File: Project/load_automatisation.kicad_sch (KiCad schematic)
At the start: 9 parts, among them IC3 MC74VHC138DR2G, J10 DadConnector, J11 TENG, J9 PowerIn, U1 AMS1117-5.0

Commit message: new schematic
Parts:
- IC3: footprint SOIC127P600X175-16N -> Library:SOIC127P600X175-16N
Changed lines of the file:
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@@
 	(wire
 		(pts
-			(xy 105.41 74.93) (xy 107.95 74.93)
-		)
-		(stroke
-			(width 0)
-			(type default)
-		)
-	)
-	(wire
-		(pts
-			(xy 102.87 64.77) (xy 107.95 64.77)
+			(xy 101.6 74.93) (xy 107.95 74.93)
 		)
 		(stroke
@@
 	(wire
 		(pts
-			(xy 102.87 69.85) (xy 107.95 69.85)
-		)
-		(stroke
-			(width 0)
-			(type default)
-		)
-	)
-	(wire
-		(pts
 			(xy 107.95 77.47) (xy 104.14 77.47)
 		)
@@
 	(wire
 		(pts
+			(xy 99.06 67.31) (xy 107.95 67.31)
+		)
+		(stroke
+			(width 0)
+			(type default)
+		)
+	)
+	(wire
+		(pts
 			(xy 115.57 39.37) (xy 115.57 36.83)
 		)
@@
 	(wire
 		(pts
-			(xy 102.87 67.31) (xy 107.95 67.31)
-		)
-		(stroke
-			(width 0)
-			(type default)
-		)
-	)
-	(wire
-		(pts
 			(xy 41.91 40.64) (xy 58.42 40.64)
 		)
@@
 	(wire
 		(pts
-			(xy 102.87 72.39) (xy 107.95 72.39)
-		)
-		(stroke
-			(width 0)
-			(type default)
-		)
-	)
-	(wire
-		(pts
-			(xy 102.87 59.69) (xy 107.95 59.69)
-		)
-		(stroke
-			(width 0)
-			(type default)
-		)
-	)
-	(wire
-		(pts
 			(xy 35.56 68.58) (xy 44.45 68.58)
 		)
@@
 	(wire
 		(pts
+			(xy 99.06 69.85) (xy 107.95 69.85)
+		)
+		(stroke
+			(width 0)
+			(type default)
+		)
+	)
+	(wire
+		(pts
 			(xy 58.42 40.64) (xy 58.42 38.1)
 		)
@@
 	(wire
 		(pts
+			(xy 99.06 62.23) (xy 107.95 62.23)
+		)
+		(stroke
+			(width 0)
+			(type default)
+		)
+	)
+	(wire
+		(pts
 			(xy 157.48 72.39) (xy 160.02 72.39)
 		)
@@
 	(wire
 		(pts
-			(xy 102.87 62.23) (xy 107.95 62.23)
-		)
-		(stroke
-			(width 0)
-			(type default)
-		)
-	)
-	(wire
-		(pts
 			(xy 35.56 71.12) (xy 44.45 71.12)
 		)
@@
 	(wire
 		(pts
+			(xy 99.06 72.39) (xy 107.95 72.39)
+		)
+		(stroke
+			(width 0)
+			(type default)
+		)
+	)
+	(wire
+		(pts
 			(xy 35.56 76.2) (xy 44.45 76.2)
 		)
@@
 	(wire
 		(pts
+			(xy 99.06 59.69) (xy 107.95 59.69)
+		)
+		(stroke
+			(width 0)
+			(type default)
+		)
+	)
+	(wire
+		(pts
 			(xy 157.48 64.77) (xy 160.02 64.77)
 		)
@@
 		(pts
 			(xy 41.91 30.48) (xy 50.8 30.48)
+		)
+		(stroke
+			(width 0)
+			(type default)
+		)
+	)
+	(wire
+		(pts
+			(xy 99.06 64.77) (xy 107.95 64.77)
 		)
 		(stroke
@@
 	)
 	(label "Y7"
-		(at 105.41 74.93 180)
+		(at 101.6 74.93 180)
 		(fields_autoplaced yes)
 		(effects
@@
 		)
 	)
+	(label "Din2"
+		(at 99.06 64.77 0)
+		(fields_autoplaced yes)
+		(effects
+			(font
+				(size 1.27 1.27)
+			)
+			(justify left bottom)
+		)
+	)
 	(label "Y6"
 		(at 135.89 77.47 0)
@@
 		)
 	)
-	(label "Din1"
-		(at 102.87 62.23 0)
-		(fields_autoplaced yes)
-		(effects
-			(font
-				(size 1.27 1.27)
-			)
-			(justify left bottom)
-		)
-	)
 	(label "Y5"
 		(at 157.48 72.39 180)
@@
 		)
 	)
+	(label "Din4"
+		(at 99.06 69.85 0)
+		(fields_autoplaced yes)
+		(effects
+			(font
+				(size 1.27 1.27)
+			)
+			(justify left bottom)
+		)
+	)
 	(label "Y2"
 		(at 157.48 64.77 180)
@@
 		)
 	)
-	(label "Din3"
-		(at 102.87 67.31 0)
-		(fields_autoplaced yes)
-		(effects
-			(font
-				(size 1.27 1.27)
-			)
-			(justify left bottom)
-		)
-	)
-	(label "Din2"
-		(at 102.87 64.77 0)
+	(label "Din1"
+		(at 99.06 62.23 0)
 		(fields_autoplaced yes)
 		(effects
@@
 		)
 	)
-	(label "Din5"
-		(at 102.87 72.39 0)
-		(fields_autoplaced yes)
-		(effects
-			(font
-				(size 1.27 1.27)
-			)
-			(justify left bottom)
-		)
-	)
 	(label "Vsense"
 		(at 181.61 73.66 0)
@@
 		)
 	)
-	(label "Din4"
-		(at 102.87 69.85 0)
-		(fields_autoplaced yes)
-		(effects
-			(font
-				(size 1.27 1.27)
-			)
-			(justify left bottom)
-		)
-	)
-	(label "Din0"
-		(at 102.87 59.69 0)
+	(label "Din5"
+		(at 99.06 72.39 0)
 		(fields_autoplaced yes)
 		(effects
@@
 			)
 			(justify right bottom)
+		)
+	)
+	(label "Din0"
+		(at 99.06 59.69 0)
+		(fields_autoplaced yes)
+		(effects
+			(font
+				(size 1.27 1.27)
+			)
+			(justify left bottom)
+		)
+	)
+	(label "Din3"
+		(at 99.06 67.31 0)
+		(fields_autoplaced yes)
+		(effects
+			(font
+				(size 1.27 1.27)
+			)
+			(justify left bottom)
 		)
 	)
@@
 			)
 		)
-		(property "Footprint" "SOIC127P600X175-16N"
+		(property "Footprint" "Library:SOIC127P600X175-16N"
 			(at 129.54 154.61 0)
 			(effects

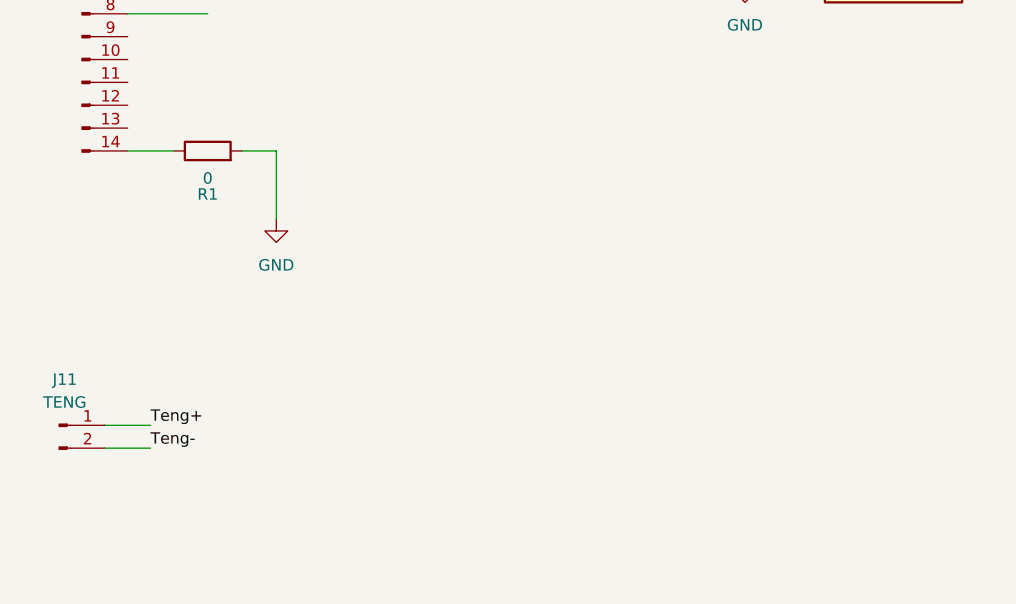
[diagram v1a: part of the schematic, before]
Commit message: update schematic
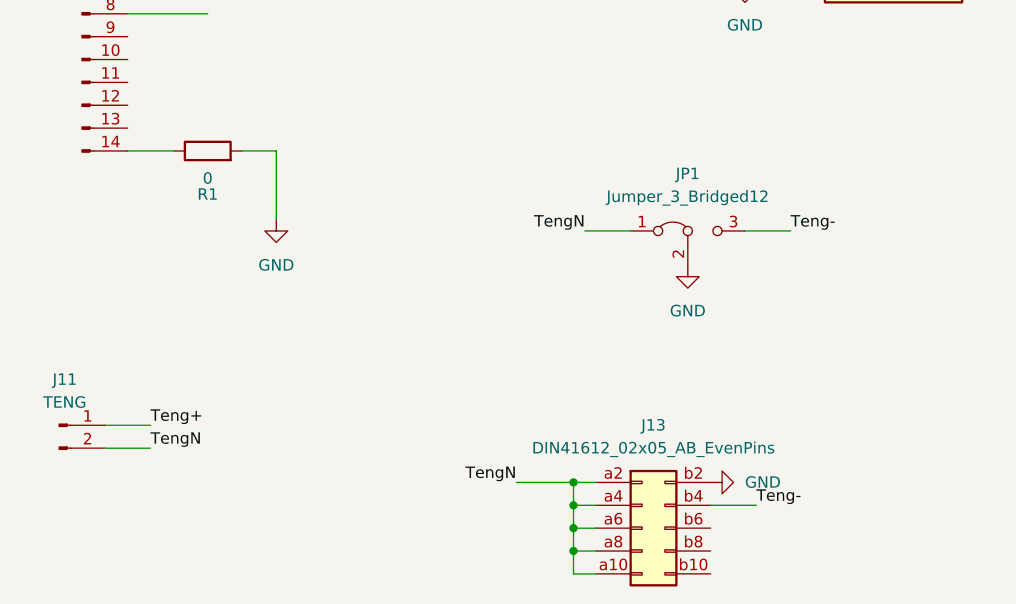
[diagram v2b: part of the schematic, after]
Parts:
- added J13: DIN41612_02x05_AB_EvenPins, Connector_PinSocket_2.54mm:PinSocket_2x05_P2.54mm_Vertical, symbol Connector:DIN41612_02x05_AB_EvenPins
- added JP1: Jumper_3_Bridged12, Connector_PinHeader_2.54mm:PinHeader_1x03_P2.54mm_Vertical, symbol Jumper:Jumper_3_Bridged12
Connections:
- net GND: now also J13.b2 (Pin_b2), JP1.2 (C)
- net Teng-: now also J13.b4 (Pin_b4), JP1.3 (B); no longer J11.2 (Pin_2)
- new net TengN: J11.2 (Pin_2), J13.a10 (Pin_a10), J13.a2 (Pin_a2), J13.a4 (Pin_a4), J13.a6 (Pin_a6), J13.a8 (Pin_a8), JP1.1 (A)

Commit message: new 24 loads 25/10
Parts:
- removed J10: DadConnector, Connector_PinHeader_2.54mm:PinHeader_1x14_P2.54mm_Vertical, symbol Connector:Conn_01x14_Pin
- removed J13: DIN41612_02x05_AB_EvenPins, Connector_PinSocket_2.54mm:PinSocket_2x05_P2.54mm_Vertical, symbol Connector:DIN41612_02x05_AB_EvenPins
- removed JP1: Jumper_3_Bridged12, Connector_PinHeader_2.54mm:PinHeader_1x03_P2.54mm_Vertical, symbol Jumper:Jumper_3_Bridged12
- added C4, C5, C6: 100nF, Capacitor_SMD:C_0805_2012Metric, symbol Device:C
- added IC1, IC10, IC2, IC6, IC7, IC8: TD62083AFGNEL, SOIC127P1030X245-18N, symbol SamacSys_Parts:TD62083AFGNEL
- added IC4, IC5: MC74VHC138DR2G, SamacSys_Parts:SOIC127P600X175-16N, symbol SamacSys_Parts:MC74VHC138DR2G
- added IC9: LM358PWG4, SOP65P640X120-8N, symbol SamacSys_Parts:LM358PWG4
- added J10: TENGConnector, 231162001000, symbol SamacSys_Parts:231-162_001-000
- added J12: PH-2X05SG, HDRV10W66P254_2X5_1270X500X895P, symbol SamacSys_Parts:PH-2X05SG
- added J19: DaqConnector, 231339001000, symbol SamacSys_Parts:231-339_001-000
- added JP2: Jumper_3_Bridged12, Jumper:SolderJumper-3_P1.3mm_Bridged2Bar12_Pad1.0x1.5mm_NumberLabels, symbol Jumper:Jumper_3_Bridged12
- added Q1, Q2: 2N5457, PN4117, symbol SamacSys_Parts:2N5457
- added R2, R3, R4, R5, R6: R, Resistor_SMD:R_0805_2012Metric, symbol Device:R
- added U2: INA128, Package_SO:SOIC-8_3.9x4.9mm_P1.27mm, symbol Amplifier_Instrumentation:INA128
- R1: value 0 -> R
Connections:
- net Din0: now also IC4.1 (A0), IC5.1 (A0), J19.1
- net Din1: now also IC4.2 (A1), IC5.2 (A1), J19.2
- net Din2: now also IC4.3 (A2), IC5.3 (A2), J19.3
- net Din3: now also IC4.4 (~{E1}), IC5.4 (~{E1}), J19.4
- net Din4: now also IC4.5 (~{E2}), IC5.5 (~{E2}), J19.5
- net Din5: now also IC4.6 (E3), IC5.6 (E3), J19.6
- net GND: now also IC1.9 (GND), IC10.9 (GND), IC2.9 (GND), IC4.8 (GND), IC5.8 (GND), IC6.9 (GND), IC7.9 (GND), IC8.9 (GND), IC9.3 (IN1+), IC9.4 (V-), J12.9, JP2.2 (C), R5.2, U2.4 (V-), U2.5 (Ref)
- net Teng+: now also J10.1
- net TengN: now also J10.2, J12.1, JP2.3 (B)
- net VCC: now also IC1.10 (COMMON), IC10.10 (COMMON), IC2.10 (COMMON), IC4.16 (VCC), IC5.16 (VCC), IC6.10 (COMMON), IC7.10 (COMMON), IC8.10 (COMMON), IC9.8 (V+), Q1.2 (D), Q2.2 (D), U2.7 (V+)
- net Vsense: now also C5.1
- net Y0: now also IC1.1 (I1), IC2.1 (I1)
- net Y1: now also IC1.2 (I2), IC2.2 (I2)
- net Y2: now also IC1.3 (I3), IC2.3 (I3)
- net Y3: now also IC1.4 (I4), IC2.4 (I4)
- net Y4: now also IC1.5 (I5), IC2.5 (I5)
- net Y5: now also IC1.6 (I6), IC2.6 (I6)
- net Y6: now also IC1.7 (I7), IC2.7 (I7)
- net Y7: now also IC1.8 (I8), IC2.8 (I8)
- net at R1.1: now also C5.2, Q1.3 (G)
- new net: Q1.1 (S), R6.1
- new net: JP2.1 (A), R3.2, U2.2 (-)
- new net: C6.1, Q2.1 (S), R5.1
- new net: Q2.3 (G), R6.2
- new net: R4.1, U2.1 (Rg)
- new net: R4.2, U2.8 (Rg)
- new net Current_Sense1: C4.1, IC9.2 (IN1-), J12.3, R2.2
- new net Current_Sense2: J12.5, R3.1, U2.3 (+)
- new net Dout1: C4.2, IC9.1 (OUT1), J19.8, R2.1
- new net Dout2: J19.9, U2.6
- new net O1: IC1.18 (O1)
- new net O10: IC2.17 (O2)
- new net O11: IC2.16 (O3)
- new net O12: IC2.15 (O4)
- new net O13: IC2.14 (O5)
- new net O14: IC2.13 (O6)
- new net O15: IC2.12 (O7)
- new net O16: IC2.11 (O8)
- new net O17: IC6.18 (O1)
- new net O18: IC6.17 (O2)
- new net O19: IC6.16 (O3)
- new net O2: IC1.17 (O2)
- new net O20: IC6.15 (O4)
- new net O21: IC6.14 (O5)
- new net O22: IC6.13 (O6)
- new net O23: IC6.12 (O7)
- new net O24: IC6.11 (O8)
- new net O25: IC7.18 (O1)
- new net O26: IC7.17 (O2)
- new net O27: IC7.16 (O3)
- new net O28: IC7.15 (O4)
- new net O29: IC7.14 (O5)
- new net O3: IC1.16 (O3)
- new net O30: IC7.13 (O6)
- new net O31: IC7.12 (O7)
- new net O32: IC7.11 (O8)
- new net O33: IC8.18 (O1)
- new net O34: IC8.17 (O2)
- new net O35: IC8.16 (O3)
- new net O36: IC8.15 (O4)
- new net O37: IC8.14 (O5)
- new net O38: IC8.13 (O6)
- new net O39: IC8.12 (O7)
- new net O4: IC1.15 (O4)
- new net O40: IC8.11 (O8)
- new net O41: IC10.18 (O1)
- new net O42: IC10.17 (O2)
- new net O43: IC10.16 (O3)
- new net O44: IC10.15 (O4)
- new net O45: IC10.14 (O5)
- new net O46: IC10.13 (O6)
- new net O47: IC10.12 (O7)
- new net O48: IC10.11 (O8)
- new net O5: IC1.14 (O5)
- new net O6: IC1.13 (O6)
- new net O7: IC1.12 (O7)
- new net O8: IC1.11 (O8)
- new net O9: IC2.18 (O1)
- new net TENG-: J12.10, J12.2, J12.4, J12.6, J12.8
- new net V_daq: C6.2, J19.7
- new net Y10: IC4.13 (~{Y2}), IC6.3 (I3), IC7.3 (I3)
- new net Y11: IC4.12 (~{Y3}), IC6.4 (I4), IC7.4 (I4)
- new net Y12: IC4.11 (~{Y4}), IC6.5 (I5), IC7.5 (I5)
- new net Y13: IC4.10 (~{Y5}), IC6.6 (I6), IC7.6 (I6)
- new net Y14: IC4.9 (~{Y6}), IC6.7 (I7), IC7.7 (I7)
- new net Y15: IC4.7 (~{Y7}), IC6.8 (I8), IC7.8 (I8)
- new net Y16: IC10.1 (I1), IC5.15 (~{Y0}), IC8.1 (I1)
- new net Y17: IC10.2 (I2), IC5.14 (~{Y1}), IC8.2 (I2)
- new net Y18: IC10.3 (I3), IC5.13 (~{Y2}), IC8.3 (I3)
- new net Y19: IC10.4 (I4), IC5.12 (~{Y3}), IC8.4 (I4)
- new net Y20: IC10.5 (I5), IC5.11 (~{Y4}), IC8.5 (I5)
- new net Y21: IC10.6 (I6), IC5.10 (~{Y5}), IC8.6 (I6)
- new net Y22: IC10.7 (I7), IC5.9 (~{Y6}), IC8.7 (I7)
- new net Y23: IC10.8 (I8), IC5.7 (~{Y7}), IC8.8 (I8)
- new net Y8: IC4.15 (~{Y0}), IC6.1 (I1), IC7.1 (I1)
- new net Y9: IC4.14 (~{Y1}), IC6.2 (I2), IC7.2 (I2)
- no-connect marks 0 -> 4
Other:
- added sheet Loads1 (Loads1.kicad_sch)
- added sheet Loads2 (Loads2.kicad_sch)
- sheet Loads ports: added O1, O10, O11, O12, O13, O14, O15, O16, O2, O3, O4, O5, O6, O7, O8, O9; removed Y0, Y1, Y2, Y3, Y4, Y5, Y6, Y7
- moved on the sheet: C3, IC3, J11

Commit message: new 08/11
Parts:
- removed C5, C6: 100nF, Capacitor_SMD:C_0805_2012Metric, symbol Device:C
- removed IC1, IC10, IC2, IC6, IC7, IC8: TD62083AFGNEL, SOIC127P1030X245-18N, symbol SamacSys_Parts:TD62083AFGNEL
- removed IC3: MC74VHC138DR2G, Library:SOIC127P600X175-16N, symbol SamacSys_Parts:MC74VHC138DR2G
- removed IC4, IC5: MC74VHC138DR2G, SamacSys_Parts:SOIC127P600X175-16N, symbol SamacSys_Parts:MC74VHC138DR2G
- removed J10: TENGConnector, 231162001000, symbol SamacSys_Parts:231-162_001-000
- removed J11: TENG, Connector_PinHeader_2.54mm:PinHeader_1x02_P2.54mm_Vertical, symbol Connector:Conn_01x02_Pin
- removed J19: DaqConnector, 231339001000, symbol SamacSys_Parts:231-339_001-000
- removed JP2: Jumper_3_Bridged12, Jumper:SolderJumper-3_P1.3mm_Bridged2Bar12_Pad1.0x1.5mm_NumberLabels, symbol Jumper:Jumper_3_Bridged12
- removed Q1, Q2: 2N5457, PN4117, symbol SamacSys_Parts:2N5457
- removed R1, R5, R6: R, Resistor_SMD:R_0805_2012Metric, symbol Device:R
- added IC1: OPA2145IDR, SOIC127P600X175-8N, symbol SamacSys_Parts:OPA2145IDR
- added J13: 1757242, 1757242, symbol SamacSys_Parts:1757242
- added J30: 1757349, SHDRRA12W103P0X508_1X12_6296X1200X875P, symbol SamacSys_Parts:1757349
- added TENG_Connector1: Conn_01x04_Pin, Connector_PinHeader_2.54mm:PinHeader_1x04_P2.54mm_Vertical, symbol Connector:Conn_01x04_Pin
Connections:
- net Din0: now also J30.8
- net Din1: now also J30.7
- net Din2: now also J30.6
- net Din3: now also J30.5
- net Din4: now also J30.4
- net Din5: now also J30.3
- net Dout1: now also J30.9
- net Dout2: now also J30.10
- net GND: now also J12.10, IC1.4 (V-); no longer J12.9
- net Teng+: now also J13.1, TENG_Connector1.1 (Pin_1), TENG_Connector1.3 (Pin_3)
- net Teng-: now also J12.2, J12.4, J12.6
- net TengN: now also J12.8, J13.2, TENG_Connector1.2 (Pin_2), TENG_Connector1.4 (Pin_4)
- net VCC: now also IC1.8 (V+)
- net V_daq: now also IC1.6 (-IN_B), IC1.7 (OUT_B), J30.2
- net Vsense: now also IC1.3 (+IN_A), J30.1
- net Current_Sense2_OUT: now reaches J12.7
- net Current_Sense2_OUT: now also J12.9, R3.2, U2.2 (-)
- net Current_Sense1 renamed Current_Sense1_IN
- net Current_Sense2 renamed Current_Sense2_IN
- removed net TENG-: J12.10, J12.2, J12.4, J12.6, J12.8
- new net: IC1.1 (OUT_A), IC1.2 (-IN_A), IC1.5 (+IN_B)
- no-connect marks 4 -> 3
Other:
- removed sheet Loads
- removed sheet Loads1
- removed sheet Loads2
- added sheet 1_Loads (1_Loads.kicad_sch)
- added sheet 2_Loads (2_Loads.kicad_sch)
- added sheet 3_Loads (3_Loads.kicad_sch)
- moved on the sheet: C1, C2, C3, C4, IC9, J12, J9, R2, R3, R4, U1, U2

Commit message: new 08/11
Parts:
- removed IC9: LM358PWG4, SOP65P640X120-8N, symbol SamacSys_Parts:LM358PWG4
- removed R2: R, Resistor_SMD:R_0805_2012Metric, symbol Device:R
- added IC12: OPA387DBVR, SOT95P280X145-5N, symbol SamacSys_Parts:OPA387DBVR
- added R1: R, Resistor_SMD:R_0805_2012Metric, symbol Device:R
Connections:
- net Current_Sense1_IN: now also IC12.4 (-IN), R1.2
- net Dout1: now also IC12.1 (OUT), R1.1
- net GND: now also IC12.2 (V-), IC12.3 (+IN)
- net VCC: now also IC12.5 (V+)
- no-connect marks 3 -> 0

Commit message: routing 25/11
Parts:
- added C10, C11, C12, C13, C14, C5, C6, C7, C8, C9: 100nF, Capacitor_SMD:C_0805_2012Metric, symbol Device:C
- added H1, H2, H3, H4: MountingHole, MountingHole:MountingHole_5.3mm_M5, symbol Mechanical:MountingHole
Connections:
- net Current_Sense1_IN: now also J12.4; no longer J12.3
- net Current_Sense2_IN: now also J12.6; no longer J12.5
- net Current_Sense2_OUT: now also J12.10, J12.8; no longer J12.7, J12.9
- net Dout1: now also J30.12; no longer J30.9
- net Dout2: now also J30.11; no longer J30.10
- net GND: now also J12.9, C10.2, C11.2, C12.2, C13.2, C14.2, C5.2, C6.2, C7.2, C8.2, C9.2; no longer J12.10
- net Teng+: now also TENG_Connector1.2 (Pin_2); no longer TENG_Connector1.3 (Pin_3)
- net Teng-: now also IC1.5 (+IN_B), J12.1, J12.3, J12.5; no longer J12.2, J12.4, J12.6
- net TengN: now also J12.2, J12.7, TENG_Connector1.3 (Pin_3); no longer J12.1, J12.8, TENG_Connector1.2 (Pin_2)
- net VCC: now also C10.1, C11.1, C12.1, C13.1, C14.1, C5.1, C6.1, C7.1, C8.1, C9.1
- net Vsense: no longer J30.1
- net V_daq+: now reaches IC1.1 (OUT_A), IC1.2 (-IN_A)
- net V_daq+: now also J30.10; no longer IC1.5 (+IN_B)
- net V_daq renamed V_daq-
- net V_daq-: now also J30.9; no longer J30.2

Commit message: routing 03/12
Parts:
- added C15, C16: 100uF, Capacitor_THT:CP_Radial_D8.0mm_P3.80mm, symbol Device:C_Polarized
- added J1: PowerNeg, Connector_PinHeader_2.54mm:PinHeader_1x02_P2.54mm_Vertical, symbol Connector:Conn_01x02_Pin
- added U3: AMS1117-5.0, Package_TO_SOT_SMD:SOT-223-3_TabPin2, symbol Regulator_Linear:AMS1117-5.0
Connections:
- net GND: now also C15.2, C16.2, J1.2 (Pin_2), U3.1 (GND); no longer IC12.2 (V-)
- new net -VCC: C16.1, IC12.2 (V-), U3.2 (VO)
- new net VNeg: C15.1, J1.1 (Pin_1), U3.3 (VI)
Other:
- moved on the sheet: C1, C2, J13, J30, J9, TENG_Connector1, U1
